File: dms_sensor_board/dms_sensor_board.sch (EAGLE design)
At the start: 20 parts

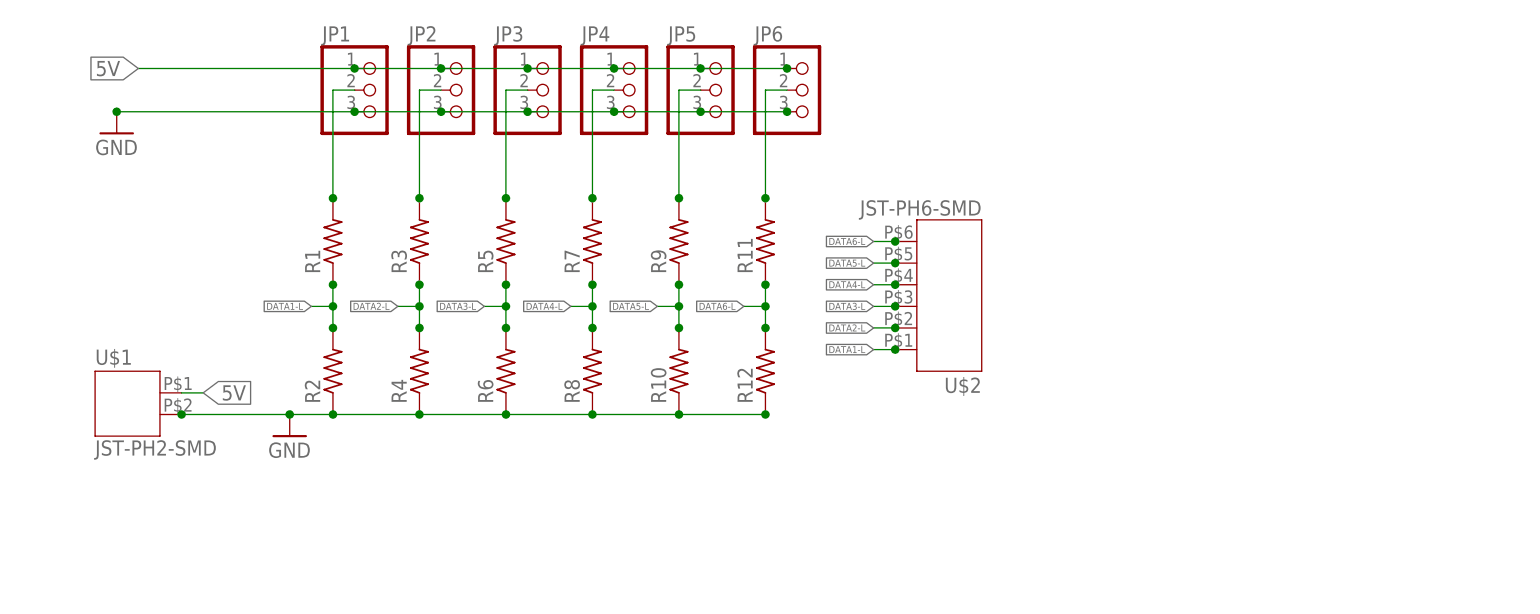
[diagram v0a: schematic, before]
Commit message: added 8b mux and started pcb
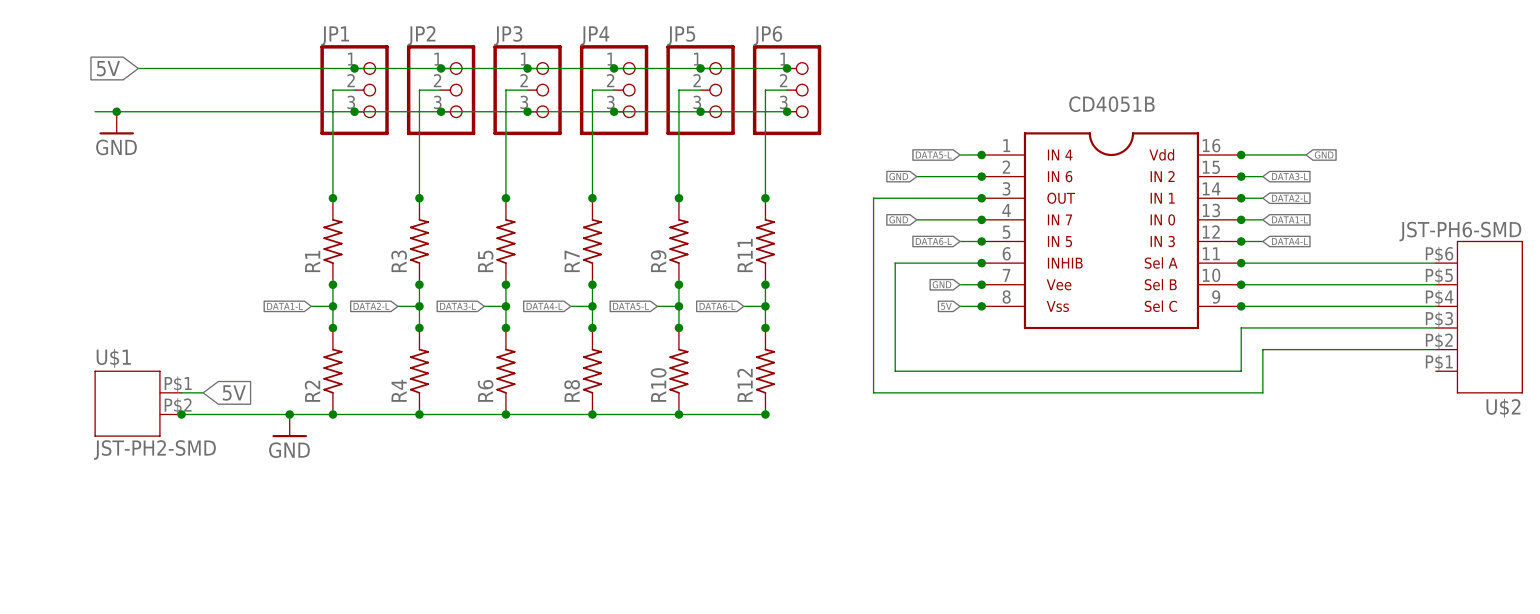
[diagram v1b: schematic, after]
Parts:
- added U$3: 8X1_ANALOG_MUX, ngohara_parts:8X1_ANALOG_MUX
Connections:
- new net N$1: U$2.6
- new net N$2: U$2.5
- new net N$3: U$2.4
- new net N$4: U$2.3
- new net N$5: U$2.2
- net DATA1-L: no longer U$2.1
- net DATA2-L: no longer U$2.2
- net DATA3-L: no longer U$2.3
- net DATA4-L: no longer U$2.4
- net DATA5-L: no longer U$2.5
- net DATA6-L: no longer U$2.6
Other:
- moved on the sheet: U$2

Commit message: added mosfet control over DMS ON
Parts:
- added Q1: IRLML5203, ngohara_parts:IRLML5203
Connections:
- new net DMS_ON: Q1.G, U$2.1
- new net N$6: U$3.P$8
- net 5V: now also Q1.D, Q1.S
- net DATA1-L: now also U$3.P$13
- net DATA2-L: now also U$3.P$14
- net DATA3-L: now also U$3.P$15
- net DATA4-L: now also U$3.P$12
- net DATA5-L: now also U$3.P$1
- net DATA6-L: now also U$3.P$5
- net GND: now also U$3.P$16, U$3.P$2, U$3.P$4, U$3.P$7
- net N$1: now also U$3.P$11
- net N$2: now also U$3.P$10
- net N$3: now also U$3.P$9
- net N$4: now also U$3.P$6
- net N$5: now also U$3.P$3
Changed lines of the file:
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@@
 <part name="GND2" library="supply1" deviceset="GND" device=""/>
 <part name="U$3" library="ngohara_parts" deviceset="8X1_ANALOG_MUX" device=""/>
+<part name="Q1" library="ngohara_parts" deviceset="IRLML5203" device=""/>
 </parts>
 <sheets>
@@
 <instance part="GND2" gate="1" x="2.54" y="45.72"/>
 <instance part="U$3" gate="G$1" x="119.38" y="33.02"/>
+<instance part="Q1" gate="G$1" x="15.24" y="53.34" smashed="yes" rot="R90">
+<attribute name="NAME" x="20.32" y="58.42" size="1.778" layer="95" rot="R180"/>
+</instance>
 </instances>
 <busses>
@@
 <junction x="104.14" y="27.94"/>
 <junction x="134.62" y="43.18"/>
+<pinref part="U$3" gate="G$1" pin="P$2"/>
+<pinref part="U$3" gate="G$1" pin="P$4"/>
+<pinref part="U$3" gate="G$1" pin="P$7"/>
+<pinref part="U$3" gate="G$1" pin="P$16"/>
 </segment>
 </net>
 <net name="5V" class="0">
+<segment>
+<wire x1="5.08" y1="55.88" x2="10.16" y2="55.88" width="0.1524" layer="91"/>
+<label x="5.08" y="55.88" size="1.778" layer="95" rot="R180" xref="yes"/>
+<pinref part="Q1" gate="G$1" pin="D"/>
+<junction x="10.16" y="55.88"/>
+</segment>
 <segment>
 <pinref part="U$1" gate="G$1" pin="1"/>
 <wire x1="10.16" y1="15.24" x2="12.7" y2="15.24" width="0.1524" layer="91"/>
 <label x="12.7" y="15.24" size="1.778" layer="95" xref="yes"/>
-<label x="5.08" y="53.34" size="1.778" layer="95" rot="R180" xref="yes"/>
+<junction x="10.16" y="15.24"/>
+</segment>
+<segment>
 <pinref part="JP1" gate="A" pin="1"/>
-<wire x1="5.08" y1="53.34" x2="30.48" y2="53.34" width="0.1524" layer="91"/>
 <pinref part="JP2" gate="A" pin="1"/>
 <wire x1="30.48" y1="53.34" x2="40.64" y2="53.34" width="0.1524" layer="91"/>
@@
 <pinref part="JP6" gate="A" pin="1"/>
 <wire x1="71.12" y1="53.34" x2="81.28" y2="53.34" width="0.1524" layer="91"/>
-<junction x="30.48" y="53.34"/>
 <junction x="40.64" y="53.34"/>
 <junction x="50.8" y="53.34"/>
@@
 <junction x="71.12" y="53.34"/>
 <junction x="81.28" y="53.34"/>
-<wire x1="104.14" y1="25.4" x2="101.6" y2="25.4" width="0.1524" layer="91"/>
-<label x="101.6" y="25.4" size="0.8128" layer="95" ratio="12" rot="R180" xref="yes"/>
-<junction x="104.14" y="25.4"/>
+<pinref part="Q1" gate="G$1" pin="S"/>
+<wire x1="20.32" y1="55.88" x2="22.86" y2="55.88" width="0.1524" layer="91"/>
+<wire x1="22.86" y1="55.88" x2="22.86" y2="53.34" width="0.1524" layer="91"/>
+<wire x1="22.86" y1="53.34" x2="30.48" y2="53.34" width="0.1524" layer="91"/>
+<junction x="20.32" y="55.88"/>
+<junction x="30.48" y="53.34"/>
 </segment>
 </net>
@@
 <wire x1="27.94" y1="50.8" x2="27.94" y2="38.1" width="0.1524" layer="91"/>
 <junction x="27.94" y="38.1"/>
+<junction x="30.48" y="50.8"/>
 </segment>
 </net>
@@
 <wire x1="38.1" y1="50.8" x2="38.1" y2="38.1" width="0.1524" layer="91"/>
 <junction x="38.1" y="38.1"/>
+<junction x="40.64" y="50.8"/>
 </segment>
 </net>
@@
 <wire x1="48.26" y1="50.8" x2="48.26" y2="38.1" width="0.1524" layer="91"/>
 <junction x="48.26" y="38.1"/>
+<junction x="50.8" y="50.8"/>
 </segment>
 </net>
@@
 <wire x1="58.42" y1="50.8" x2="58.42" y2="38.1" width="0.1524" layer="91"/>
 <junction x="58.42" y="38.1"/>
+<junction x="60.96" y="50.8"/>
 </segment>
 </net>
@@
 <wire x1="68.58" y1="50.8" x2="68.58" y2="38.1" width="0.1524" layer="91"/>
 <junction x="68.58" y="38.1"/>
+<junction x="71.12" y="50.8"/>
 </segment>
 </net>
@@
 <wire x1="78.74" y1="50.8" x2="78.74" y2="38.1" width="0.1524" layer="91"/>
 <junction x="78.74" y="38.1"/>
+<junction x="81.28" y="50.8"/>
 </segment>
 </net>
@@
 <label x="137.16" y="35.56" size="0.8128" layer="95" ratio="12" xref="yes"/>
 <junction x="134.62" y="35.56"/>
+<pinref part="U$3" gate="G$1" pin="P$13"/>
 </segment>
 </net>
@@
 <label x="137.16" y="38.1" size="0.8128" layer="95" ratio="12" xref="yes"/>
 <junction x="134.62" y="38.1"/>
+<pinref part="U$3" gate="G$1" pin="P$14"/>
 </segment>
 </net>
@@
 <label x="137.16" y="40.64" size="0.8128" layer="95" ratio="12" xref="yes"/>
 <junction x="134.62" y="40.64"/>
+<pinref part="U$3" gate="G$1" pin="P$15"/>
 </segment>
 </net>
@@
 <label x="137.16" y="33.02" size="0.8128" layer="95" ratio="12" xref="yes"/>
 <junction x="134.62" y="33.02"/>
+<pinref part="U$3" gate="G$1" pin="P$12"/>
 </segment>
 </net>
@@
 <label x="101.6" y="43.18" size="0.8128" layer="95" ratio="12" rot="R180" xref="yes"/>
 <junction x="104.14" y="43.18"/>
+<pinref part="U$3" gate="G$1" pin="P$1"/>
 </segment>
 </net>
@@
 <label x="101.6" y="33.02" size="0.8128" layer="95" ratio="12" rot="R180" xref="yes"/>
 <junction x="104.14" y="33.02"/>
+<pinref part="U$3" gate="G$1" pin="P$5"/>
 </segment>
 </net>
@@
 <wire x1="134.62" y1="30.48" x2="157.48" y2="30.48" width="0.1524" layer="91"/>
 <junction x="134.62" y="30.48"/>
+<junction x="157.48" y="30.48"/>
+<pinref part="U$3" gate="G$1" pin="P$11"/>
 </segment>
 </net>
@@
 <wire x1="134.62" y1="27.94" x2="157.48" y2="27.94" width="0.1524" layer="91"/>
 <junction x="134.62" y="27.94"/>
+<junction x="157.48" y="27.94"/>
+<pinref part="U$3" gate="G$1" pin="P$10"/>
 </segment>
 </net>
@@
 <wire x1="134.62" y1="25.4" x2="157.48" y2="25.4" width="0.1524" layer="91"/>
 <junction x="134.62" y="25.4"/>
+<junction x="157.48" y="25.4"/>
+<pinref part="U$3" gate="G$1" pin="P$9"/>
 </segment>
 </net>
@@
 <wire x1="134.62" y1="22.86" x2="157.48" y2="22.86" width="0.1524" layer="91"/>
 <junction x="104.14" y="30.48"/>
+<junction x="157.48" y="22.86"/>
+<pinref part="U$3" gate="G$1" pin="P$6"/>
 </segment>
 </net>
@@
 <wire x1="137.16" y1="20.32" x2="157.48" y2="20.32" width="0.1524" layer="91"/>
 <junction x="104.14" y="38.1"/>
-</segment>
-</net>
+<junction x="157.48" y="20.32"/>
+<pinref part="U$3" gate="G$1" pin="P$3"/>
+</segment>
+</net>
+<net name="N$6" class="0">
+<segment>
+<junction x="104.14" y="25.4"/>
+<pinref part="U$3" gate="G$1" pin="P$8"/>
+<wire x1="104.14" y1="25.4" x2="101.6" y2="25.4" width="0.1524" layer="91"/>
+<label x="101.6" y="25.4" size="0.8128" layer="95" ratio="12" rot="R180" xref="yes"/>
+</segment>
+</net>
+<net name="DMS_ON" class="0">
+<segment>
+<pinref part="Q1" gate="G$1" pin="G"/>
+<wire x1="12.7" y1="50.8" x2="5.08" y2="50.8" width="0.1524" layer="91"/>
+<label x="5.08" y="50.8" size="1.6764" layer="95" ratio="7" rot="R180" xref="yes"/>
+<wire x1="157.48" y1="17.78" x2="152.4" y2="17.78" width="0.1524" layer="91"/>
+<label x="152.4" y="17.78" size="1.6764" layer="95" ratio="7" rot="R180" xref="yes"/>
+<pinref part="U$2" gate="G$1" pin="1"/>
+<junction x="157.48" y="17.78"/>
+<junction x="12.7" y="50.8"/>
+</segment>
+</net>

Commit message: Finished dms sensor board layout, needs DRC
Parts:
- MUX1: value 8X1_ANALOG_MUX -> 8X1
- renumbered U$3 to MUX1
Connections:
- removed net N$6: MUX1.P$8
- new net VCC: JP1.1, JP2.1, JP3.1, JP4.1, JP5.1, JP6.1, Q1.S
- net 5V: now also MUX1.P$8; no longer JP1.1, JP2.1, JP3.1, JP4.1, JP5.1, JP6.1, Q1.S

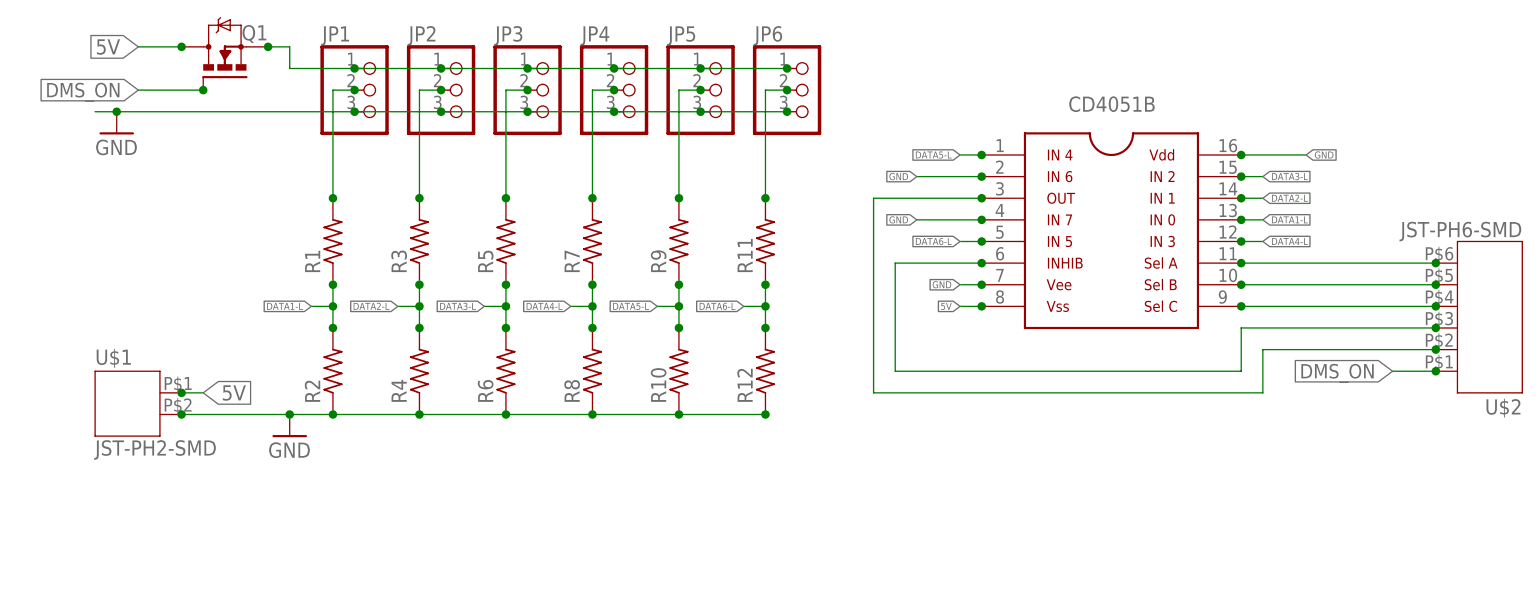
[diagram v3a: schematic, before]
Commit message: Fixed DMS_on fet with resistors and finished text
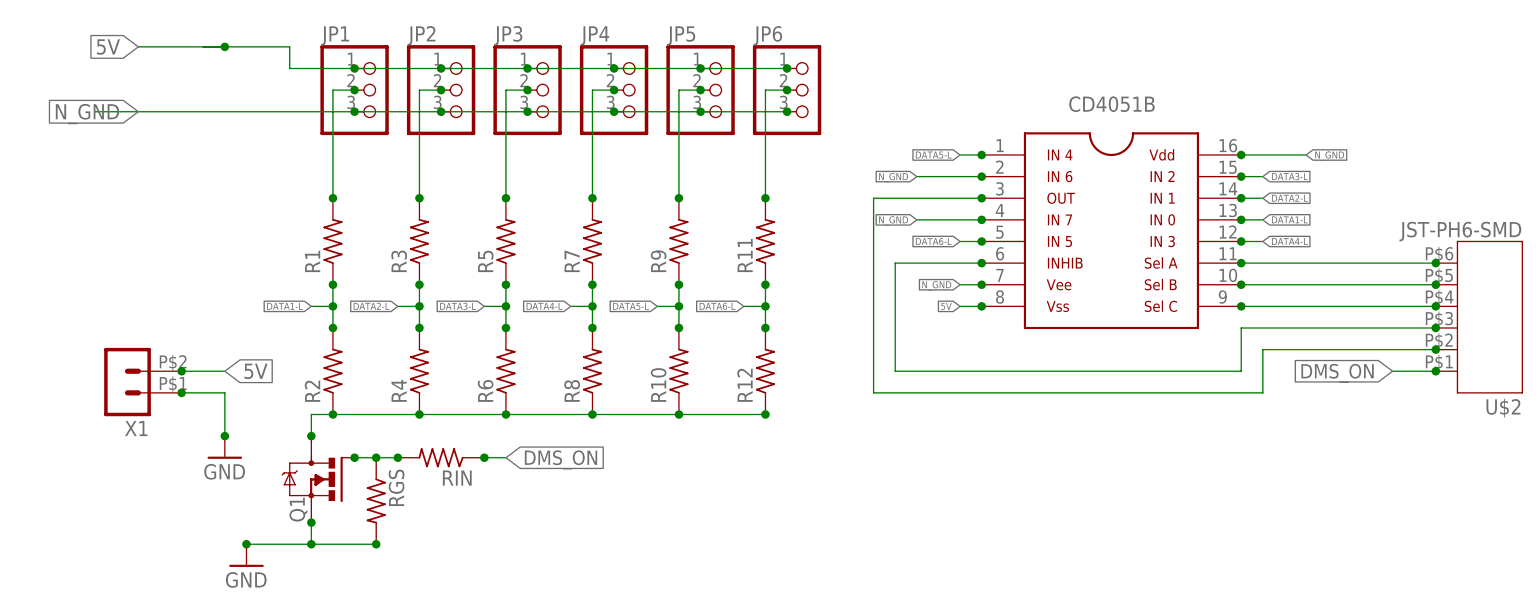
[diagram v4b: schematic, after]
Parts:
- removed U$1: JST-PH2-SMD, jst-ph:JST-PH2-SMD
- added RGS, RIN: (no value), resistor:R-US_R0805
- added X1: (no value), con-molex-micro-fit-3_0:HEADER_POS2_43045-0206
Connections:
- removed net VCC: JP1.1, JP2.1, JP3.1, JP4.1, JP5.1, JP6.1, Q1.S
- new net N$8: Q1.G, RGS.1, RIN.2
- new net N_GND: JP1.3, JP2.3, JP3.3, JP4.3, JP5.3, JP6.3, MUX1.P$16, MUX1.P$2, MUX1.P$4, MUX1.P$7, Q1.D, R10.1, R12.1, R2.1, R4.1, R6.1, R8.1
- net 5V: now also JP1.1, JP2.1, JP3.1, JP4.1, JP5.1, JP6.1, X1.2; no longer Q1.D, U$1.1
- net DMS_ON: now also RIN.1; no longer Q1.G
- net GND: now also Q1.S, RGS.2, X1.1; no longer JP1.3, JP2.3, JP3.3, JP4.3, JP5.3, JP6.3, MUX1.P$16, MUX1.P$2, MUX1.P$4, MUX1.P$7, R10.1, R12.1, R2.1, R4.1, R6.1, R8.1, U$1.2
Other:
- moved on the sheet: Q1
